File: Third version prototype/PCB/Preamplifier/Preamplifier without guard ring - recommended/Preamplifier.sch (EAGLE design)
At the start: 140 parts, among them IC1 AD8066, IC2 ADG701BRTZN, IC3 AD8066, IC4 AD8066, IC5 LT1713, IC6 LT1713, IC7 AD8066, X1 87437-0443, X2 87437-0443, X3 87437-0443

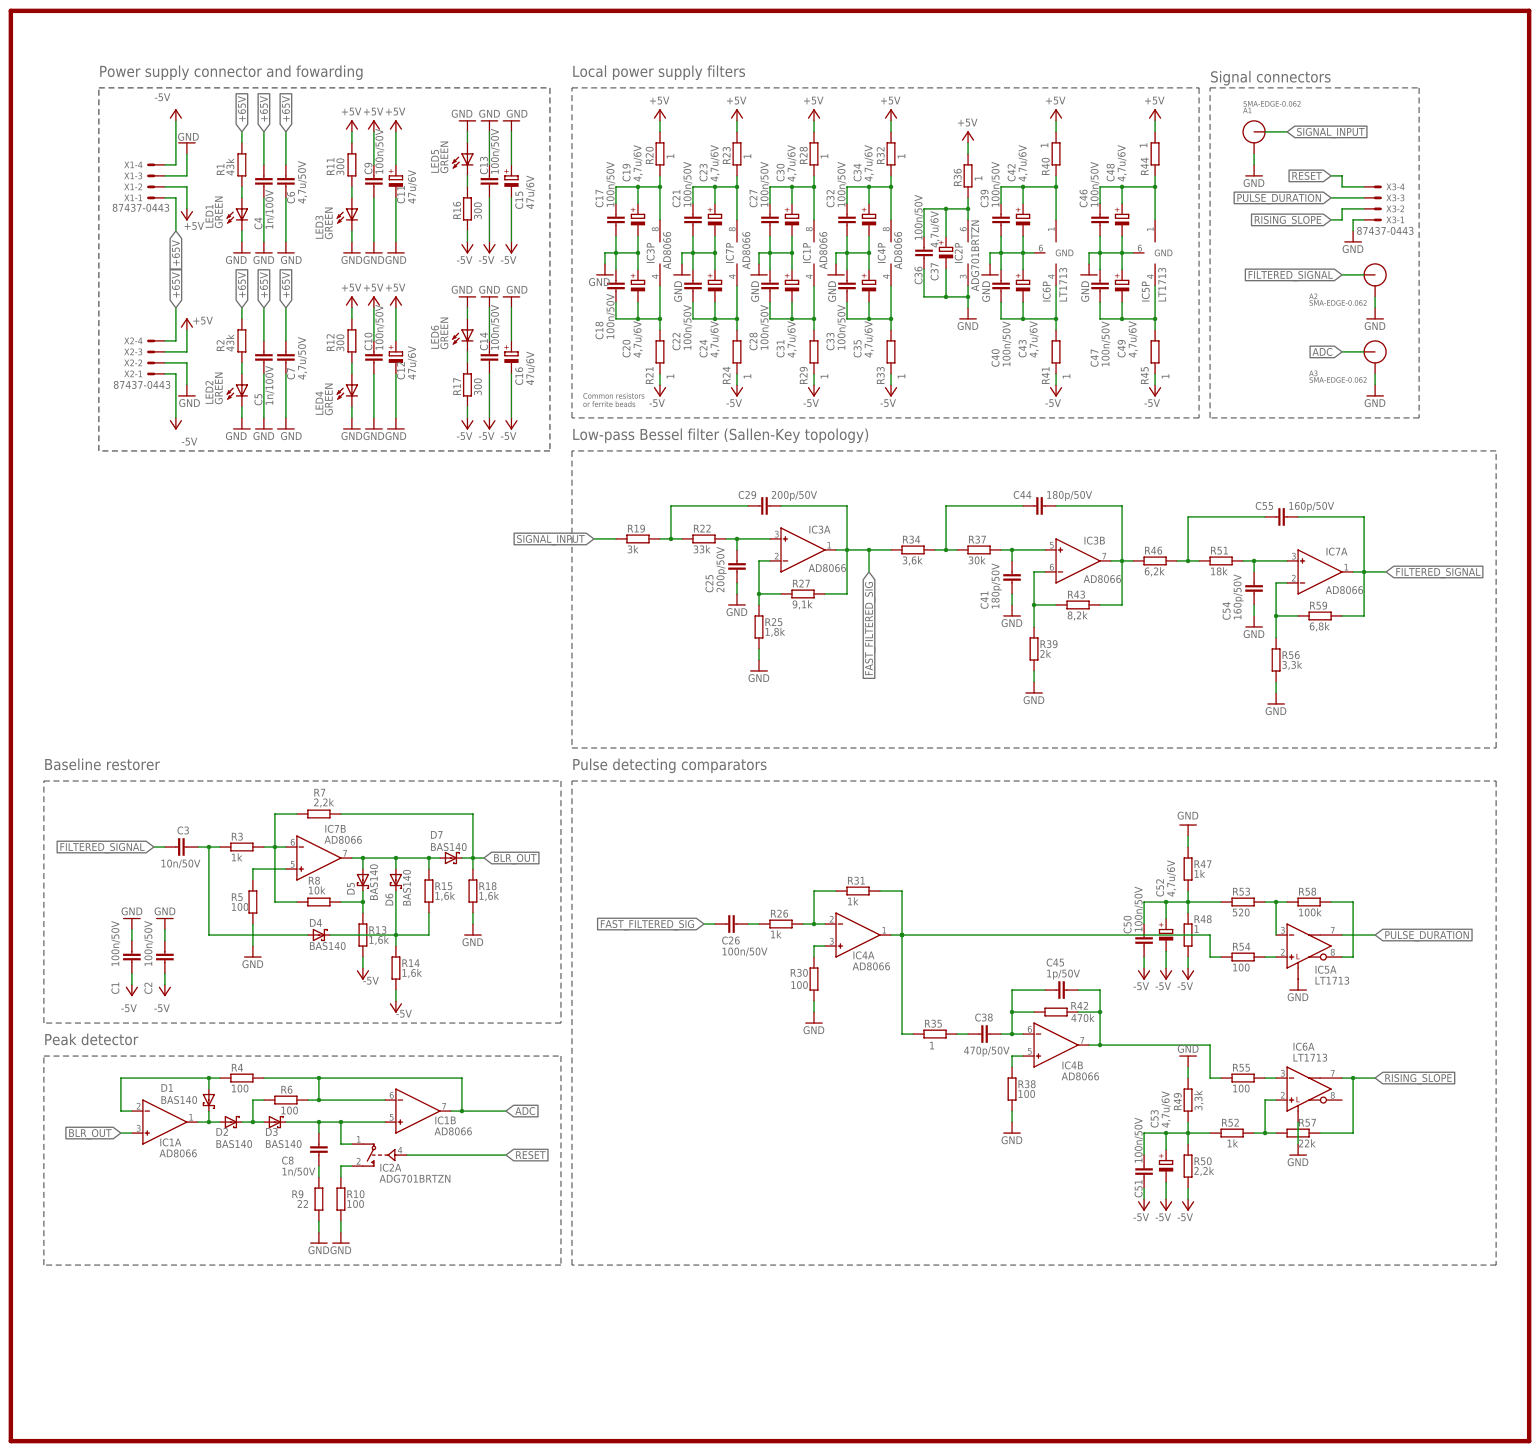
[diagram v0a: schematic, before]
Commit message: Removed guard ring due to ocurring shorts and adjusted supply rail resistors
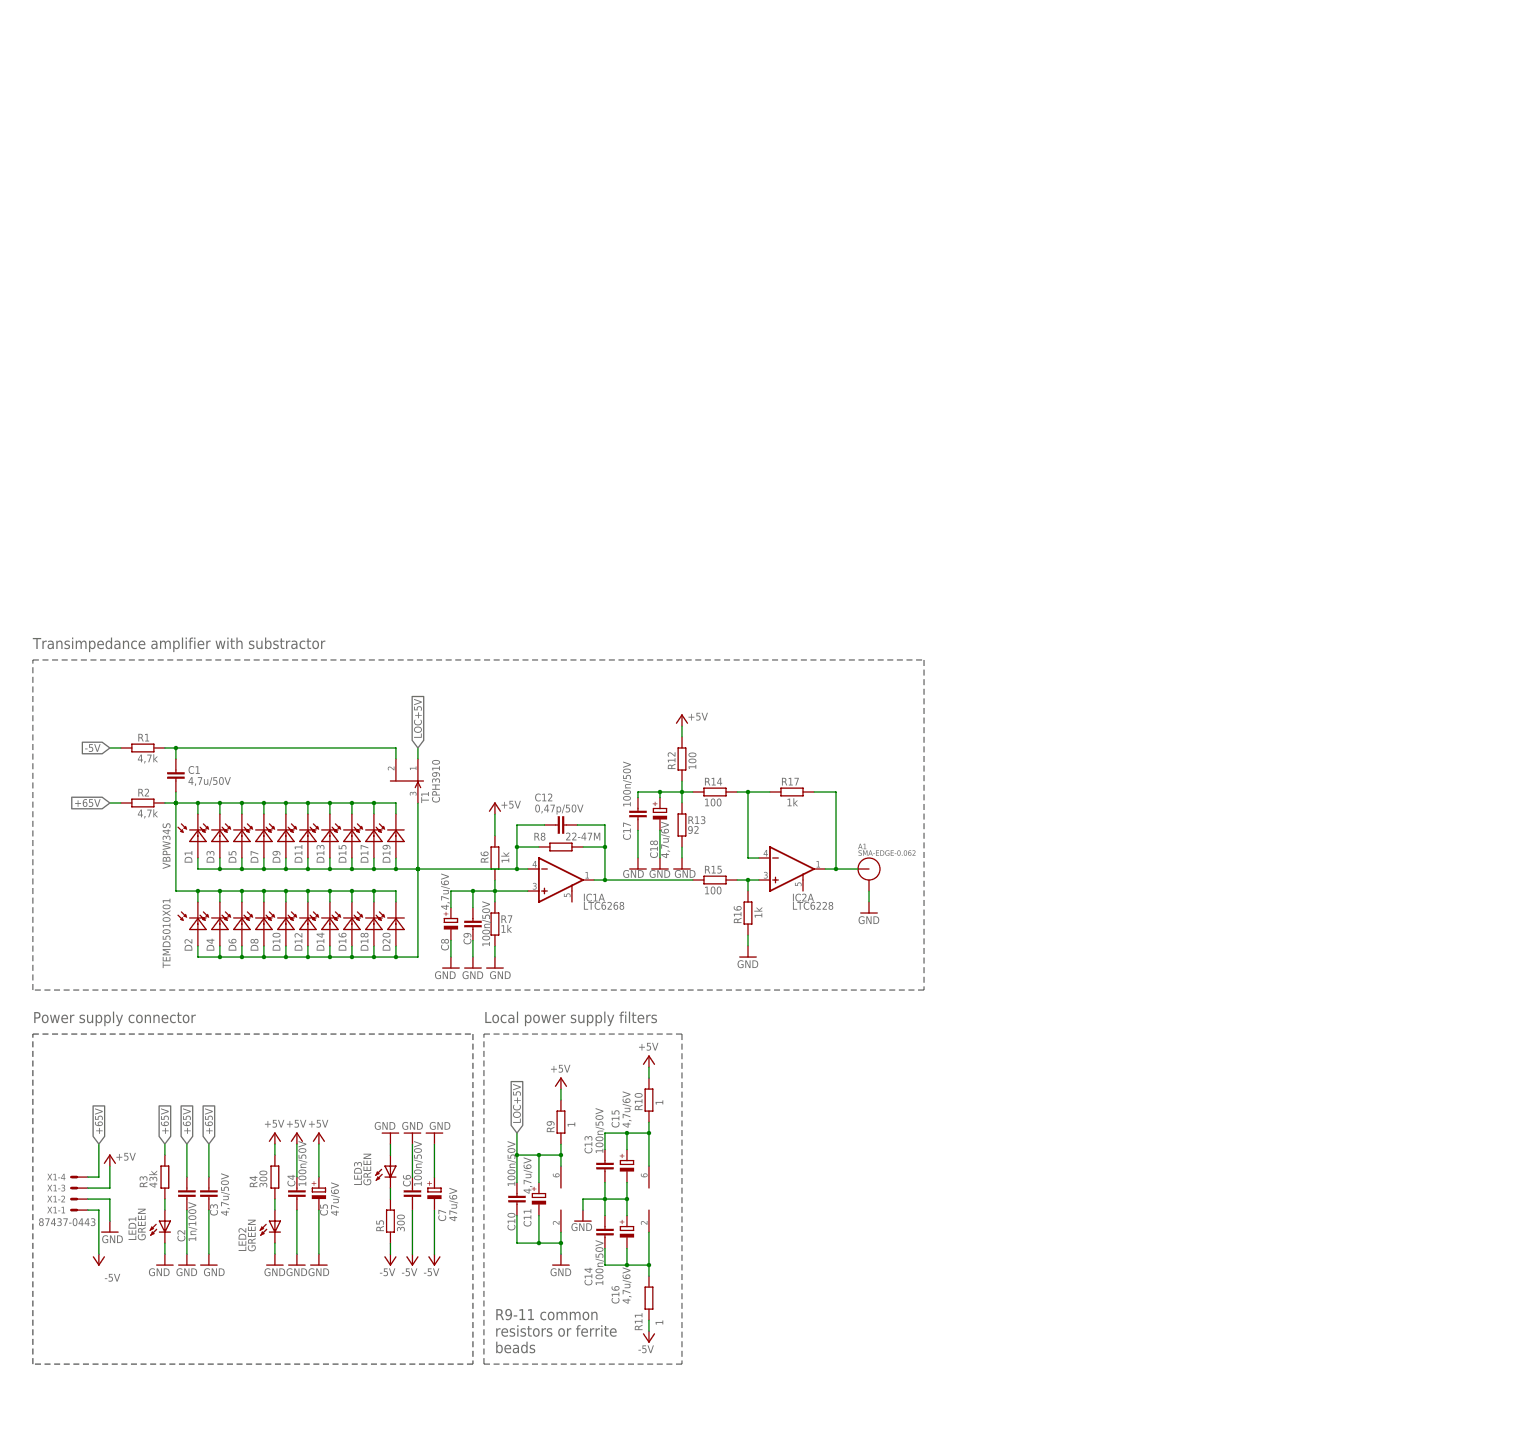
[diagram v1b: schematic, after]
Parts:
- removed A2, A3: SMA-EDGE-0.062, connector:LINX-SMA-EDGE-0.062
- removed C19, C20, C23, C24, C30, C31, C34, C35, C37, C42, C43, C48, C49, C52, C53: 4,7u/6V, rcl:CPOL-EUSMCA
- removed C21, C22, C26, C27, C28, C32, C33, C36, C39, C40, C46, C47, C50, C51: 100n/50V, rcl:C-EUC0603
- removed C25, C29: 200p/50V, rcl:C-EUC0603
- removed C38: 470p/50V, rcl:C-EUC0603
- removed C41, C44: 180p/50V, rcl:C-EUC0603
- removed C45: 1p/50V, rcl:C-EUC0603
- removed C54, C55: 160p/50V, rcl:C-EUC0603
- removed IC3, IC4, IC7: AD8066, analog-devices:AD8066
- removed IC5, IC6: LT1713, analog-devices:LT1713
- removed LED4, LED5, LED6: GREEN, led:LEDCHIPLED_0603
- removed R18: 1,6k, rcl:R-EU_R0603
- removed R19: 3k, rcl:R-EU_R0603
- removed R20, R21, R23, R24, R28, R29, R32, R33, R35, R36, R40, R41, R44, R45, R48: 1, rcl:R-EU_R0603
- removed R22: 33k, rcl:R-EU_R0603
- removed R25: 1,8k, rcl:R-EU_R0603
- removed R26, R31, R47, R52: 1k, rcl:R-EU_R0603
- removed R27: 9,1k, rcl:R-EU_R0603
- removed R30, R38, R54, R55: 100, rcl:R-EU_R0603
- removed R34: 3,6k, rcl:R-EU_R0603
- removed R37: 30k, rcl:R-EU_R0603
- removed R39: 2k, rcl:R-EU_R0603
- removed R42: 470k, rcl:R-EU_R0603
- removed R43: 8,2k, rcl:R-EU_R0603
- removed R46: 6,2k, rcl:R-EU_R0603
- removed R49, R56: 3,3k, rcl:R-EU_R0603
- removed R50: 2,2k, rcl:R-EU_R0603
- removed R51: 18k, rcl:R-EU_R0603
- removed R53: 520, rcl:R-EU_R0603
- removed R57: 22k, rcl:R-EU_R0603
- removed R58: 100k, rcl:R-EU_R0603
- removed R59: 6,8k, rcl:R-EU_R0603
- removed X2, X3: 87437-0443, con-molex:87438-0487437-0443
- added D10, D12, D14, D16, D18, D20, D8: TEMD5010X01, TEMD5010X01:TEMD5010X01
- added D11, D13, D15, D17, D19, D9: VBPW34S, VBPW34S:VBPW34S
- added T1: CPH3910, CPH3910:CPH3910
- C1: value 100n/50V -> 4,7u/50V; device rcl:C-EUC0603 -> rcl:C-EUC1206
- C11, C15, C16: value 47u/6V -> 4,7u/6V; device rcl:CPOL-EUSMCB -> rcl:CPOL-EUSMCA
- C12: value 47u/6V -> 0,47p/50V; device rcl:CPOL-EUSMCB -> rcl:C-EUC0603
- C18: value 100n/50V -> 4,7u/6V; device rcl:C-EUC0603 -> rcl:CPOL-EUSMCA
- C2: value 100n/50V -> 1n/100V
- C3: value 10n/50V -> 4,7u/50V; device rcl:C-EUC0603 -> rcl:C-EUC1206
- C4: value 1n/100V -> 100n/50V
- C5: value 1n/100V -> 47u/6V; device rcl:C-EUC0603 -> rcl:CPOL-EUSMCB
- C6: value 4,7u/50V -> 100n/50V; device rcl:C-EUC1206 -> rcl:C-EUC0603
- C7: value 4,7u/50V -> 47u/6V; device rcl:C-EUC1206 -> rcl:CPOL-EUSMCB
- C8: value 1n/50V -> 4,7u/6V; device rcl:C-EUC0603 -> rcl:CPOL-EUSMCA
- D1, D3, D5, D7: value BAS140 -> VBPW34S; device NXP_60_26022015:BAS140 -> VBPW34S:VBPW34S
- D2, D4, D6: value BAS140 -> TEMD5010X01; device NXP_60_26022015:BAS140 -> TEMD5010X01:TEMD5010X01
- IC1: value AD8066 -> LTC6268; device analog-devices:AD8066 -> LTC6268:LTC6268
- IC2: value ADG701BRTZN -> LTC6228; device ADG701BRTZ:ADG701BRTZN -> LTC6268:LTC6268
- R1, R2: value 43k -> 4,7k
- R10: value 100 -> 1
- R11: value 300 -> 1
- R12: value 300 -> 100
- R13: value 1,6k -> 92
- R14, R15: value 1,6k -> 100
- R16, R17: value 300 -> 1k
- R3: value 1k -> 43k
- R4, R5: value 100 -> 300
- R6: value 100 -> 1k
- R7: value 2,2k -> 1k
- R8: value 10k -> 22-47M
- R9: value 22 -> 1
- X1: value 87437-0443 -> 87437-0443
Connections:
- removed net ADC: A3.ANT, IC1B.IN-, IC1B.OUT, R4.2, R6.2
- removed net BLR_OUT: D7.K, IC1A.IN+, R18.1, R7.1
- removed net FAST_FILTERED_SIG: C26.2, C29.1, IC3A.OUT, R27.2, R34.1
- removed net FILTERED_SIGNAL: A2.ANT, C3.2, C55.1, IC7A.OUT, R59.2
- removed net N$10: C29.2, R19.2, R22.1
- removed net N$11: C3.1, D4.A, R3.1
- removed net N$12: IC7B.IN-, R3.2, R7.2, R8.2
- removed net N$13: D5.A, D6.A, D7.A, IC7B.OUT, R15.1
- removed net N$14: D1.K, D2.A, IC1A.OUT
- removed net N$15: C25.2, IC3A.IN+, R22.2
- removed net N$16: IC3A.IN-, R25.2, R27.1
- removed net N$17: C27.2, C30.+, IC1P.V+, R28.2
- removed net N$18: C21.2, C23.+, IC7P.V+, R23.2
- removed net N$19: C44.2, R34.2, R37.1
- removed net N$20: D5.K, R13.1, R8.1
- removed net N$21: C28.1, C31.-, IC1P.V-, R29.1
- removed net N$22: D4.K, D6.K, R14.1, R15.2
- removed net N$23: D1.A, IC1A.IN-, R4.1
- removed net N$24: C55.2, R46.2, R51.1
- removed net N$25: D2.K, D3.A, R6.1
- removed net N$26: IC7B.IN+, R5.2
- removed net N$28: IC4A.IN-, R26.2, R31.1
- removed net N$31: C8.1, D3.K, IC1B.IN+, IC2A.D
- removed net N$32: C41.2, IC3B.IN+, R37.2
- removed net N$33: IC3B.IN-, R39.2, R43.1
- removed net N$35: C8.2, R9.2
- removed net N$36: C54.2, IC7A.IN+, R51.2
- removed net N$39: C36.2, C37.+, IC2P.V+, R36.2
- removed net N$40: IC2A.S, R10.2
- removed net N$41: C26.1, R26.1
- removed net N$42: C39.2, C42.+, IC6P.V+, R40.2
- removed net N$43: IC4B.IN+, R38.2
- removed net N$44: C40.1, C43.-, IC6P.V-, R41.1
- removed net N$45: C46.2, C48.+, IC5P.V+, R44.2
- removed net N$46: C47.1, C49.-, IC5P.V-, R45.1
- removed net N$49: IC7A.IN-, R56.2, R59.1
- removed net N$51: IC4A.OUT, R31.2, R35.1, R54.1
- removed net N$52: IC4A.IN+, R30.2
- removed net N$53: C38.2, R35.2
- removed net N$54: C38.1, C45.2, IC4B.IN-, R42.1
- removed net N$55: C45.1, IC4B.OUT, R42.2, R55.1
- removed net N$56: IC5A.IN+, R54.2
- removed net N$57: IC6A.IN+, R52.2, R57.1
- removed net N$58: C51.1, C53.+, R49.2, R50.1, R52.1
- removed net N$59: IC5A.IN-, R53.2, R58.1
- removed net N$6: C22.1, C24.-, IC7P.V-, R24.1
- removed net N$60: IC5A.BOUT, R58.2
- removed net N$61: IC6A.IN-, R55.2
- removed net N$62: C32.2, C34.+, IC4P.V+, R32.2
- removed net N$63: C50.1, C52.+, R47.2, R48.1, R53.1
- removed net N$64: C33.1, C35.-, IC4P.V-, R33.1
- removed net N$99: C44.1, IC3B.OUT, R43.2, R46.1
- removed net PULSE_DURATION: IC5A.OUT, X3-3.S
- removed net RESET: IC2A.IN, X3-4.S
- removed net RISING_SLOPE: IC6A.OUT, R57.2, X3-2.S
- removed net SIGNAL_INPUT: A1.ANT, R19.1
- new net LOC+5V: C10.2, C11.+, IC1P.VDD, R9.2, T1.S
- new net N$29: LED2.A, R4.1
- new net N$30: LED3.C, R5.2
- new net N$47: C12.2, D1.A, D10.A, D11.A, D12.A, D13.A, D14.A, D15.A, D16.A, D17.A, D18.A, D19.A, D2.A, D20.A, D3.A, D4.A, D5.A, D6.A, D7.A, D8.A, D9.A, IC1A.-IN, R8.2, T1.G
- new net N$48: C1.1, D1.C, D10.C, D11.C, D12.C, D13.C, D14.C, D15.C, D16.C, D17.C, D18.C, D19.C, D2.C, D20.C, D3.C, D4.C, D5.C, D6.C, D7.C, D8.C, D9.C, R2.2
- new net N$8: IC2A.-IN, R14.2, R17.1
- new net N$9: C17.1, C18.+, R12.1, R13.2, R14.1
- net +5V: now also C4.2, C5.+, R10.1, R4.2, R6.2, R9.1, X1-3.S; no longer C10.2, C11.+, C12.+, C9.2, R11.2, R20.1, R23.1, R28.1, R32.1, R36.1, R40.1, R44.1, X1-2.S, X2-3.S
- net +65V: now also C2.2, C3.1, R2.1, R3.2, X1-4.S; no longer C4.2, C5.2, C6.1, C7.1, R1.2, R2.2, X1-1.S, X2-4.S
- net -5V: now also C6.1, C7.-, R1.1, R11.2, R5.1, X1-1.S; no longer C1.1, C13.1, C14.1, C15.-, C16.-, C2.1, C50.2, C51.2, C52.-, C53.-, R13.2, R14.2, R16.1, R17.1, R21.2, R24.2, R29.2, R33.2, R41.2, R45.2, R48.2, R50.2, X1-4.S, X2-1.S
- net GND: now also C13.1, C15.-, C17.2, C18.-, C2.1, C3.2, C5.-, C7.+, C8.-, IC1P.GND, LED3.A, R13.1, R16.2, R7.1, X1-2.S; no longer A2.P$2, A3.P$2, C1.2, C12.-, C13.2, C15.+, C17.1, C18.2, C19.-, C2.2, C20.+, C21.1, C22.2, C23.-, C24.+, C25.1, C27.1, C28.2, C30.-, C31.+, C32.1, C33.2, C34.-, C35.+, C36.1, C37.-, C39.1, C40.2, C41.1, C42.-, C43.+, C46.1, C47.2, C48.-, C49.+, C5.1, C54.1, C7.2, IC2P.V-, IC5A.L, IC5GND.GND, IC6A.L, IC6GND.GND, LED3.C, LED4.C, LED5.A, LED6.A, R10.1, R18.2, R25.1, R30.1, R38.1, R39.1, R47.1, R49.1, R5.1, R56.1, R9.1, X1-3.S, X2-2.S, X3-1.S
- net N$1: now also IC2A.+IN, R15.1, R16.1; no longer LED3.A, R11.1
- net N$2: now also C1.2, R1.2, T1.D; no longer LED5.C, R16.2
- net N$27: now also R3.1; no longer R1.1
- net N$3: now also C8.+, C9.2, IC1A.+IN, R6.1, R7.2; no longer LED2.A, R2.1
- net N$38: now also C13.2, C15.+, IC2P.VDD, R10.2; no longer C17.2, C19.+, IC3P.V+, R20.2
- net N$4: now also C14.1, C16.-, IC2P.GND, R11.1; no longer C18.1, C20.-, IC3P.V-, R21.1
- net N$5: now also A1.ANT, IC2A.OUT, R17.2; no longer LED4.A, R12.1
- net N$7: now also C12.1, IC1A.OUT, R15.2, R8.1; no longer LED6.C, R17.2
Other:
- note added: "Power supply connector"
- note added: "R9-11 common resistors or ferrite beads"
- note added: "Transimpedance amplifier with substractor"
- note removed: "Baseline restorer"
- note removed: "Common resistors or ferrite beads"
- note removed: "Low-pass Bessel filter (Sallen-Key topology)"
- note removed: "Peak detector"
- note removed: "Power supply connector and fowarding"
- note removed: "Pulse detecting comparators"
- note removed: "Signal connectors"
- moved on the sheet: A1, C1, C10, C11, C13, C14, C15, C16, C17, C2, C3, C4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
